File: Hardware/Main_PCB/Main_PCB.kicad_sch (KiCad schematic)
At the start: 0 parts

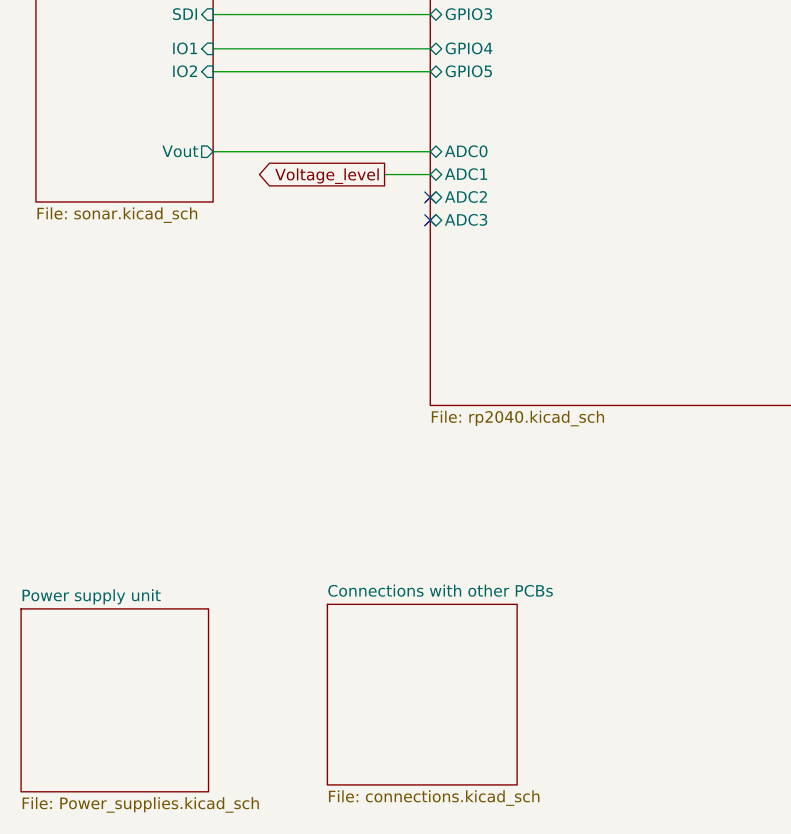
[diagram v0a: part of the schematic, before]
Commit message: Added footprints to all components
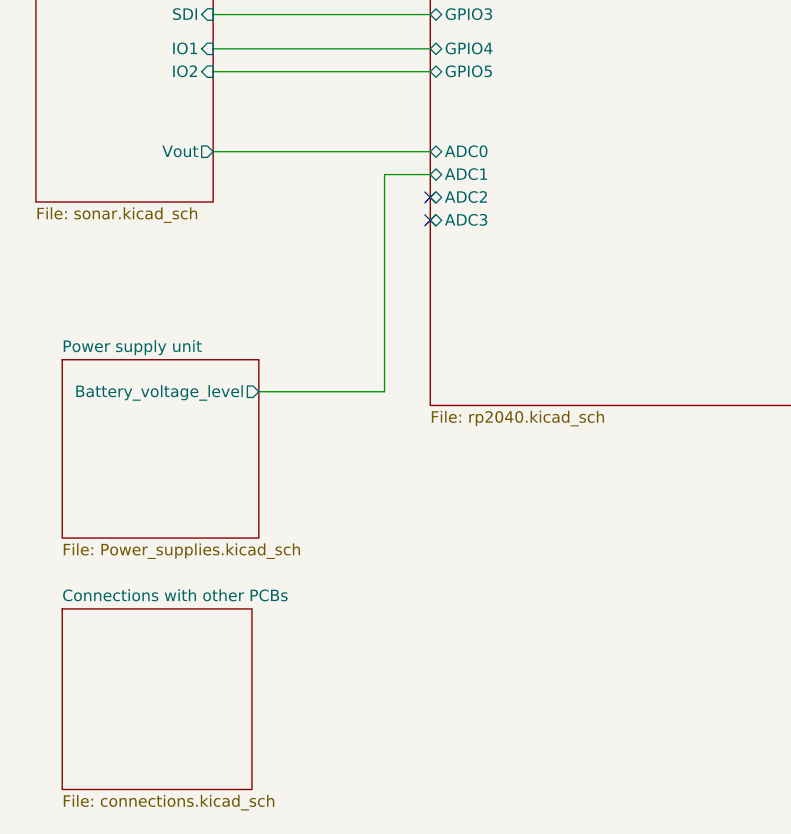
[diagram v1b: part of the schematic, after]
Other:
- sheet Power supply unit ports: added Battery_voltage_level; removed none
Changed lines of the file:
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@@
+	(wire
+		(pts
+			(xy 62.23 48.26) (xy 62.23 72.39)
+		)
+		(stroke
+			(width 0)
+			(type default)
+		)
+	)
 	(wire
 		(pts
@@
 	(wire
 		(pts
+			(xy 48.26 72.39) (xy 62.23 72.39)
+		)
+		(stroke
+			(width 0)
+			(type default)
+		)
+	)
+	(wire
+		(pts
 			(xy 43.18 25.4) (xy 67.31 25.4)
 		)
@@
 			(width 0)
 			(type default)
-		)
-	)
-	(global_label "Voltage_level"
-		(shape output)
-		(at 62.23 48.26 180)
-		(fields_autoplaced yes)
-		(effects
-			(font
-				(size 1.27 1.27)
-				(thickness 0.1588)
-			)
-			(justify right)
-		)
-		(property "Intersheetrefs" "${INTERSHEET_REFS}"
-			(at 46.7869 48.26 0)
-			(effects
-				(font
-					(size 1.27 1.27)
-				)
-				(justify right)
-				(hide yes)
-			)
 		)
 	)
@@
 	)
 	(sheet
-		(at 55.88 96.012)
+		(at 26.416 96.52)
 		(size 21.082 20.066)
 		(exclude_from_sim no)
@@
 		)
 		(property "Sheetname" "Connections with other PCBs"
-			(at 55.88 95.3004 0)
+			(at 26.416 95.8084 0)
 			(effects
 				(font
@@
 		)
 		(property "Sheetfile" "connections.kicad_sch"
-			(at 55.88 116.6626 0)
+			(at 26.416 117.1706 0)
 			(effects
 				(font
@@
 	)
 	(sheet
-		(at 21.844 96.52)
-		(size 20.828 20.32)
+		(at 26.416 68.834)
+		(size 21.844 19.812)
 		(exclude_from_sim no)
 		(in_bom yes)
@@
 		)
 		(property "Sheetname" "Power supply unit"
-			(at 21.844 95.8084 0)
+			(at 26.416 68.1224 0)
 			(effects
 				(font
@@
 		)
 		(property "Sheetfile" "Power_supplies.kicad_sch"
-			(at 21.844 117.4246 0)
+			(at 26.416 89.2306 0)
 			(effects
 				(font
@@
 			)
 		)
+		(pin "Battery_voltage_level" output
+			(at 48.26 72.39 0)
+			(effects
+				(font
+					(size 1.27 1.27)
+				)
+				(justify right)
+			)
+		)

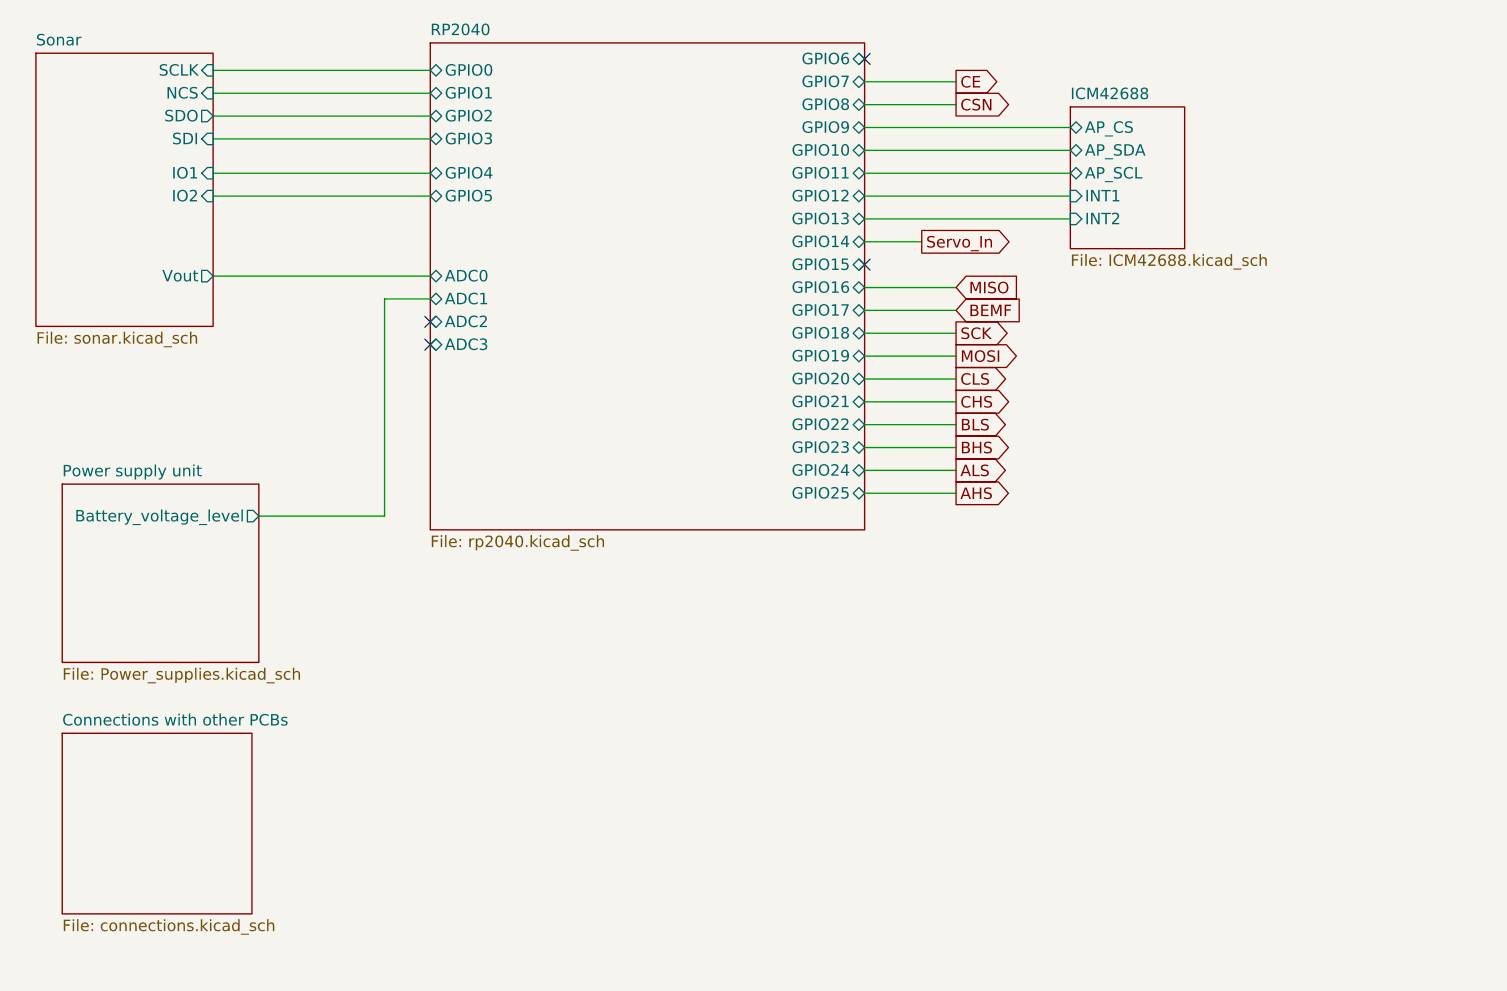
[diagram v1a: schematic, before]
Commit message: Finished the schematic of the MainPCB
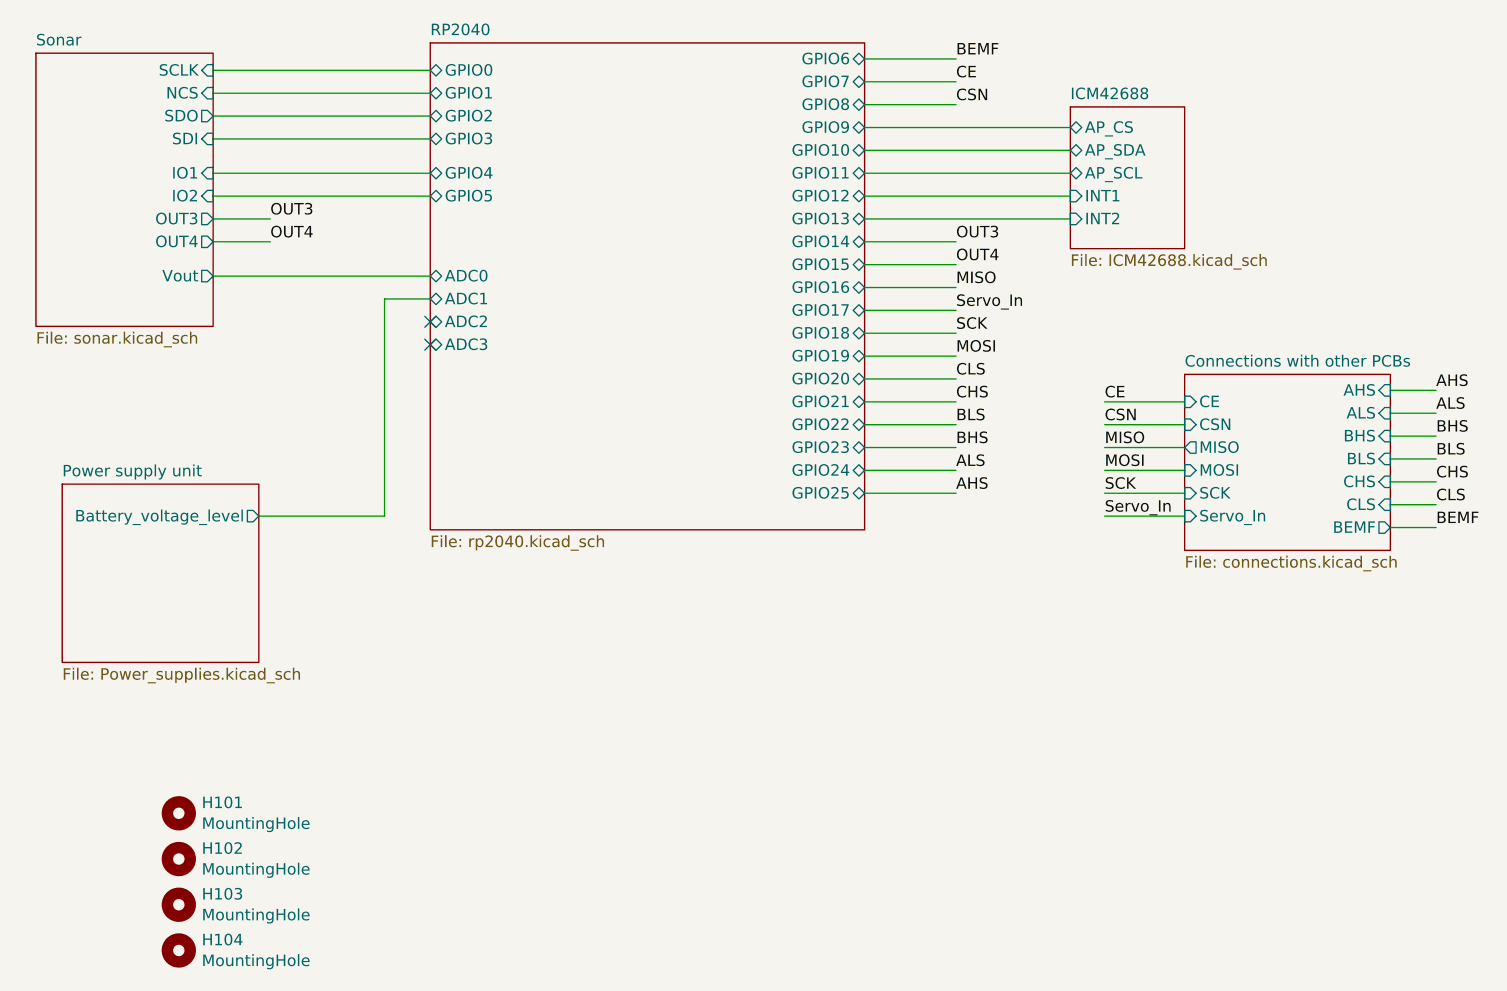
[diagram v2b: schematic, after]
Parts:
- added H101, H102, H103, H104: MountingHole, MountingHole:MountingHole_2.7mm_M2.5, symbol Mechanical:MountingHole
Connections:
- no-connect marks 4 -> 2
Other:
- sheet Connections with other PCBs ports: added AHS, ALS, BEMF, BHS, BLS, CE, CHS, CLS, CSN, MISO, MOSI, SCK, Servo_In; removed none
- sheet Sonar ports: added OUT3, OUT4; removed none

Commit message: Minor adjustments to MainPCB
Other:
- sheet ICM42688 renamed MPU6050
- sheet MPU6050 ports: added none; removed AP_CS, INT2
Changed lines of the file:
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@@
-	(wire
-		(pts
-			(xy 115.57 39.37) (xy 138.43 39.37)
-		)
-		(stroke
-			(width 0)
-			(type default)
-		)
-	)
 	(wire
 		(pts
@@
 		(pts
 			(xy 115.57 34.29) (xy 138.43 34.29)
-		)
-		(stroke
-			(width 0)
-			(type default)
-		)
-	)
-	(wire
-		(pts
-			(xy 115.57 29.21) (xy 138.43 29.21)
 		)
 		(stroke
@@
 			(color 0 0 0 0.0000)
 		)
-		(property "Sheetname" "ICM42688"
+		(property "Sheetname" "MPU6050"
 			(at 138.43 26.2124 0)
 			(effects
@@
 			)
 		)
-		(pin "AP_CS" bidirectional
-			(at 138.43 29.21 180)
-			(effects
-				(font
-					(size 1.27 1.27)
-				)
-				(justify left)
-			)
-		)
 		(pin "AP_SCL" bidirectional
 			(at 138.43 34.29 180)
@@
 			(effects
 				(font
-					(size 1.27 1.27)
-				)
-				(justify left)
-			)
-		)
-		(pin "INT2" input
-			(at 138.43 39.37 180)
-			(effects
-				(font

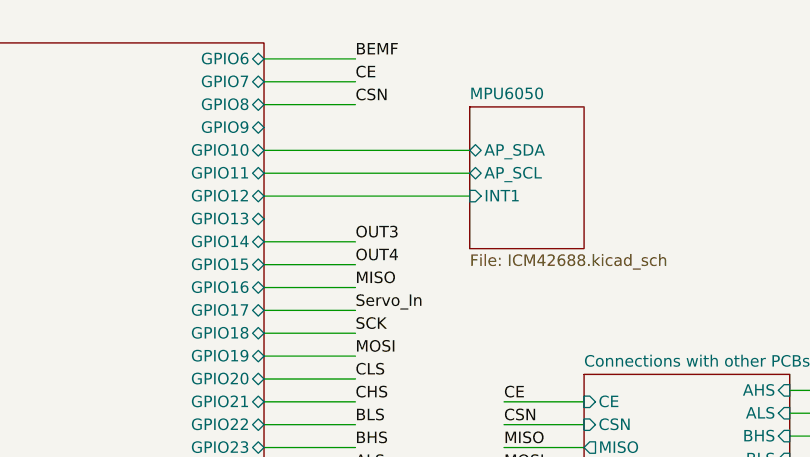
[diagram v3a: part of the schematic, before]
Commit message: Reverted to the previous IMU
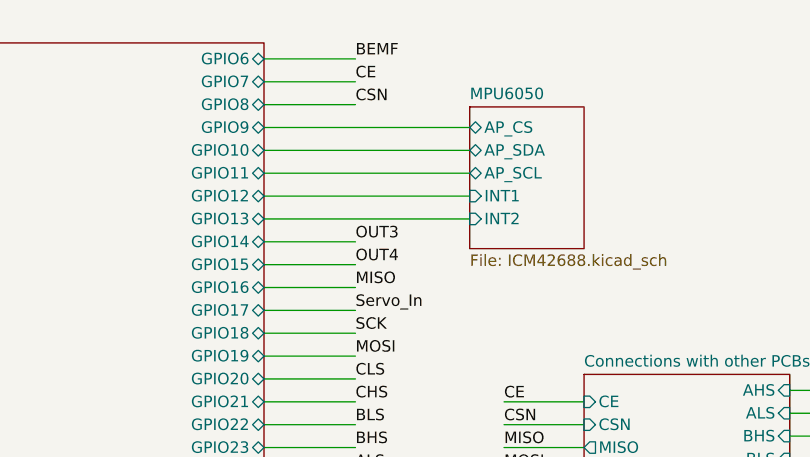
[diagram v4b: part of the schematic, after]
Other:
- sheet MPU6050 ports: added AP_CS, INT2; removed none
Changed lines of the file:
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@@
+	(wire
+		(pts
+			(xy 115.57 29.21) (xy 138.43 29.21)
+		)
+		(stroke
+			(width 0)
+			(type default)
+		)
+	)
 	(wire
 		(pts
@@
 		(pts
 			(xy 43.18 45.72) (xy 67.31 45.72)
+		)
+		(stroke
+			(width 0)
+			(type default)
+		)
+	)
+	(wire
+		(pts
+			(xy 115.57 39.37) (xy 138.43 39.37)
 		)
 		(stroke
@@
 			(effects
 				(font
+					(size 1.27 1.27)
+				)
+				(justify left)
+			)
+		)
+		(pin "AP_CS" bidirectional
+			(at 138.43 29.21 180)
+			(effects
+				(font
+					(size 1.27 1.27)
+				)
+				(justify left)
+			)
+		)
+		(pin "INT2" input
+			(at 138.43 39.37 180)
+			(effects
+				(font

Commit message: Footprint updated
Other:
- sheet MPU6050 renamed ICM42688 - Gyro
- sheet Sonar renamed TUSS4470 - SONAR
- sheet ICM42688 - Gyro ports: added AP_SDO; removed INT2
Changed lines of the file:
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@@
 			(color 0 0 0 0.0000)
 		)
-		(property "Sheetname" "MPU6050"
+		(property "Sheetname" "ICM42688 - Gyro"
 			(at 138.43 26.2124 0)
 			(effects
@@
 			)
 		)
-		(pin "INT1" input
+		(pin "INT1" output
 			(at 138.43 36.83 180)
 			(effects
@@
 			)
 		)
-		(pin "INT2" input
+		(pin "AP_SDO" bidirectional
 			(at 138.43 39.37 180)
 			(effects
@@
 			(color 0 0 0 0.0000)
 		)
-		(property "Sheetname" "Sonar"
+		(property "Sheetname" "TUSS4470 - SONAR"
 			(at 23.495 20.2434 0)
 			(effects

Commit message: Beautifying the Master Controller
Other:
- company: (none) -> Made by Liubomir Stanev
- title: (none) -> Master controller
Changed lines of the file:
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@@
 	(generator_version "9.0")
 	(paper "A5")
+	(title_block
+		(title "Master controller")
+		(date "22/12/2025")
+		(company "Made by Liubomir Stanev")
+		(comment 1 "Page 1: Connections")
+	)
 	(no_connect
 		(at 67.31 50.8)
